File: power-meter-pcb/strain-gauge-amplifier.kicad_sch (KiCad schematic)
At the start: 19 parts, among them J5 Side A, J6 Side B, Q3 AS2302, U7 ADS1232IPW

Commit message: Cleaning up PCB back and title box
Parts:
- C12, C13, C14, C15, J5, J6, NT2, Q3, R17, R18, R19, R20, SG1, SG2, SG3, SG4, U7: PlaceOnSecondary (none) -> Yes
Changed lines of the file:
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@@
 	(title_block
 		(title "Cycling power meter FYP - Strain gauge amplifier")
-		(date "2024-04-18")
+		(date "2024-05-14")
+		(rev "V1.0")
 		(company "Monash Human Power - Jotham Gates & Oscar Varney")
-		(comment 1 "For the secondary crank, set J3 to short pins 2 and 3 and short J1 and J2.")
 	)
 	(junction
@@
 			)
 		)
+		(property "PlaceOnSecondary" "Yes"
+			(at 55.88 72.39 0)
+			(effects
+				(font
+					(size 1.27 1.27)
+				)
+				(hide yes)
+			)
+		)
 		(pin "2"
 		)
@@
 			)
 		)
+		(property "PlaceOnSecondary" "Yes"
+			(at 109.22 72.39 0)
+			(effects
+				(font
+					(size 1.27 1.27)
+				)
+				(hide yes)
+			)
+		)
 		(pin "2"
 		)
@@
 			)
 		)
+		(property "PlaceOnSecondary" "Yes"
+			(at 185.42 87.63 0)
+			(effects
+				(font
+					(size 1.27 1.27)
+				)
+				(hide yes)
+			)
+		)
 		(pin "1"
 		)
@@
 			)
 		)
+		(property "PlaceOnSecondary" "Yes"
+			(at 66.04 124.46 0)
+			(effects
+				(font
+					(size 1.27 1.27)
+				)
+				(hide yes)
+			)
+		)
 		(pin "1"
 		)
@@
 			)
 		)
+		(property "PlaceOnSecondary" "Yes"
+			(at 109.22 87.63 0)
+			(effects
+				(font
+					(size 1.27 1.27)
+				)
+				(hide yes)
+			)
+		)
 		(pin "2"
 		)
@@
 			)
 		)
+		(property "PlaceOnSecondary" "Yes"
+			(at 185.42 97.79 0)
+			(effects
+				(font
+					(size 1.27 1.27)
+				)
+				(hide yes)
+			)
+		)
 		(pin "2"
 		)
@@
 			)
 		)
+		(property "PlaceOnSecondary" "Yes"
+			(at 55.88 87.63 0)
+			(effects
+				(font
+					(size 1.27 1.27)
+				)
+				(hide yes)
+			)
+		)
 		(pin "2"
 		)
@@
 			)
 		)
+		(property "PlaceOnSecondary" "Yes"
+			(at 127 88.9 0)
+			(effects
+				(font
+					(size 1.27 1.27)
+				)
+				(hide yes)
+			)
+		)
 		(pin "1"
 		)
@@
 			)
 		)
+		(property "PlaceOnSecondary" "Yes"
+			(at 68.58 78.74 0)
+			(effects
+				(font
+					(size 1.27 1.27)
+				)
+				(hide yes)
+			)
+		)
 		(pin "3"
 		)
@@
 			)
 		)
+		(property "PlaceOnSecondary" "Yes"
+			(at 153.67 130.81 0)
+			(effects
+				(font
+					(size 1.27 1.27)
+				)
+				(hide yes)
+			)
+		)
 		(pin "1"
 		)
@@
 			)
 		)
+		(property "PlaceOnSecondary" "Yes"
+			(at 236.22 91.44 0)
+			(effects
+				(font
+					(size 1.27 1.27)
+				)
+				(hide yes)
+			)
+		)
 		(pin "1"
 		)
@@
 			)
 		)
+		(property "PlaceOnSecondary" "Yes"
+			(at 224.79 91.44 0)
+			(effects
+				(font
+					(size 1.27 1.27)
+				)
+				(hide yes)
+			)
+		)
 		(pin "1"
 		)
@@
 			)
 		)
+		(property "PlaceOnSecondary" "Yes"
+			(at 96.52 78.74 0)
+			(effects
+				(font
+					(size 1.27 1.27)
+				)
+				(hide yes)
+			)
+		)
 		(pin "3"
 		)
@@
 			)
 		)
+		(property "PlaceOnSecondary" "Yes"
+			(at 59.69 118.11 0)
+			(effects
+				(font
+					(size 1.27 1.27)
+				)
+				(hide yes)
+			)
+		)
 		(pin "1"
 		)
@@
 			)
 		)
+		(property "PlaceOnSecondary" "Yes"
+			(at 156.21 100.33 0)
+			(effects
+				(font
+					(size 1.27 1.27)
+				)
+				(hide yes)
+			)
+		)
 		(pin "18"
 		)
@@
 			)
 		)
+		(property "PlaceOnSecondary" "Yes"
+			(at 73.66 118.11 0)
+			(effects
+				(font
+					(size 1.27 1.27)
+				)
+				(hide yes)
+			)
+		)
 		(pin "1"
 		)
@@
 			(at 185.42 90.17 0)
 			(effects
+				(font
+					(size 1.27 1.27)
+				)
+				(hide yes)
+			)
+		)
+		(property "PlaceOnSecondary" "Yes"
+			(at 185.42 90.17 0)
+			(effects

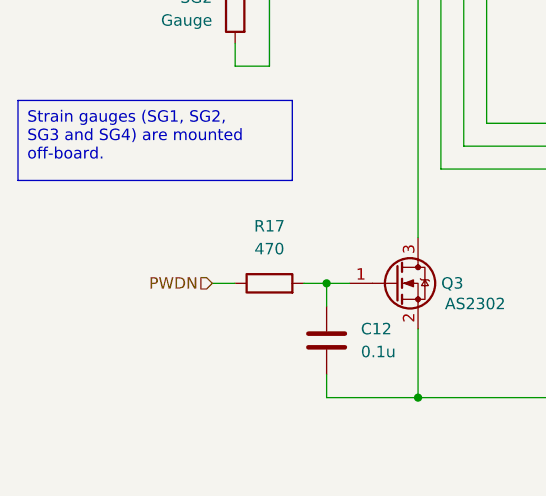
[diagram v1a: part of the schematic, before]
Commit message: Smaller PCB design started
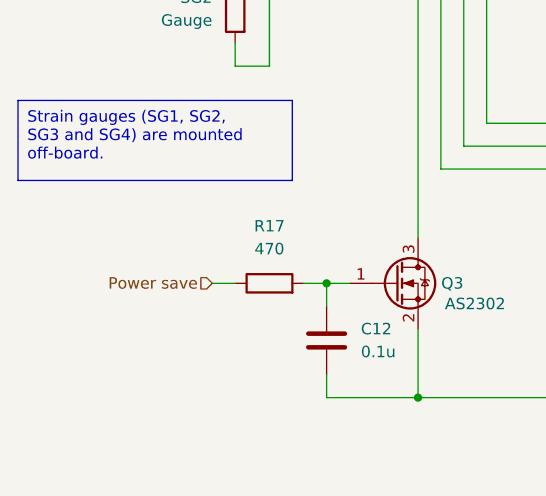
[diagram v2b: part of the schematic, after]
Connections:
- net PWDN: no longer R17.1
- new net Power save: R17.1
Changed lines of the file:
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@@
 		)
 	)
-	(hierarchical_label "PWDN"
+	(hierarchical_label "Power save"
 		(shape input)
 		(at 53.34 118.11 180)

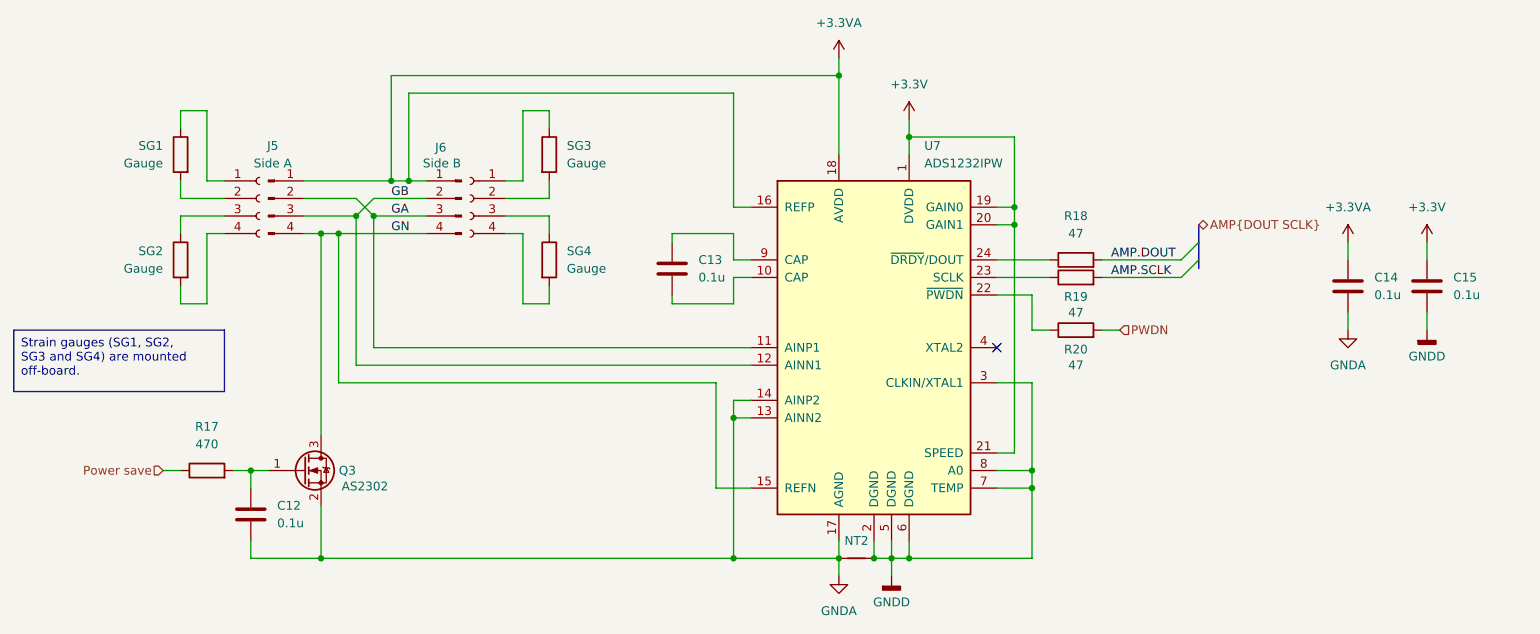
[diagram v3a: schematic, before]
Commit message: Re-centred schematics, added header for spare GPIO pins, touched up logos
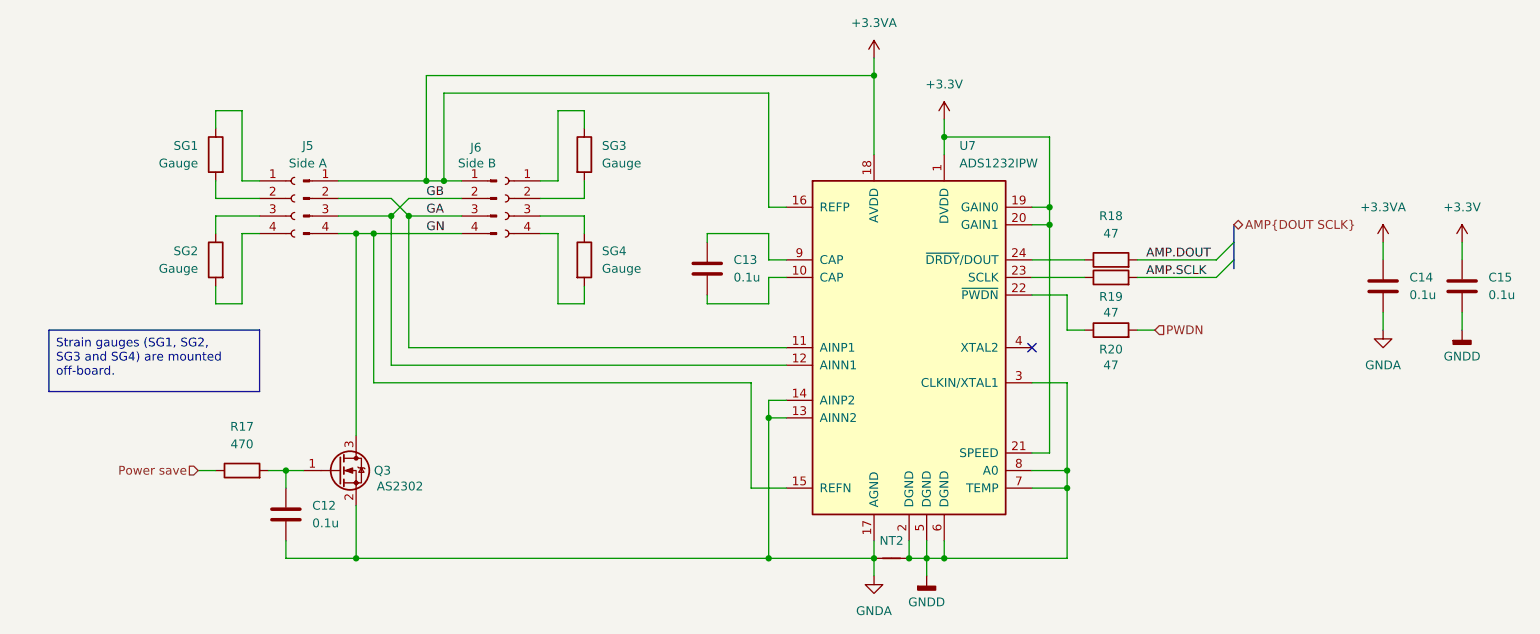
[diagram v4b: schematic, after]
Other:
- moved on the sheet: C12, C13, C14, C15, J5, J6, NT2, Q3, R17, R18, R19, R20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

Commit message: Added LED driven by temp sensor, updated numbering
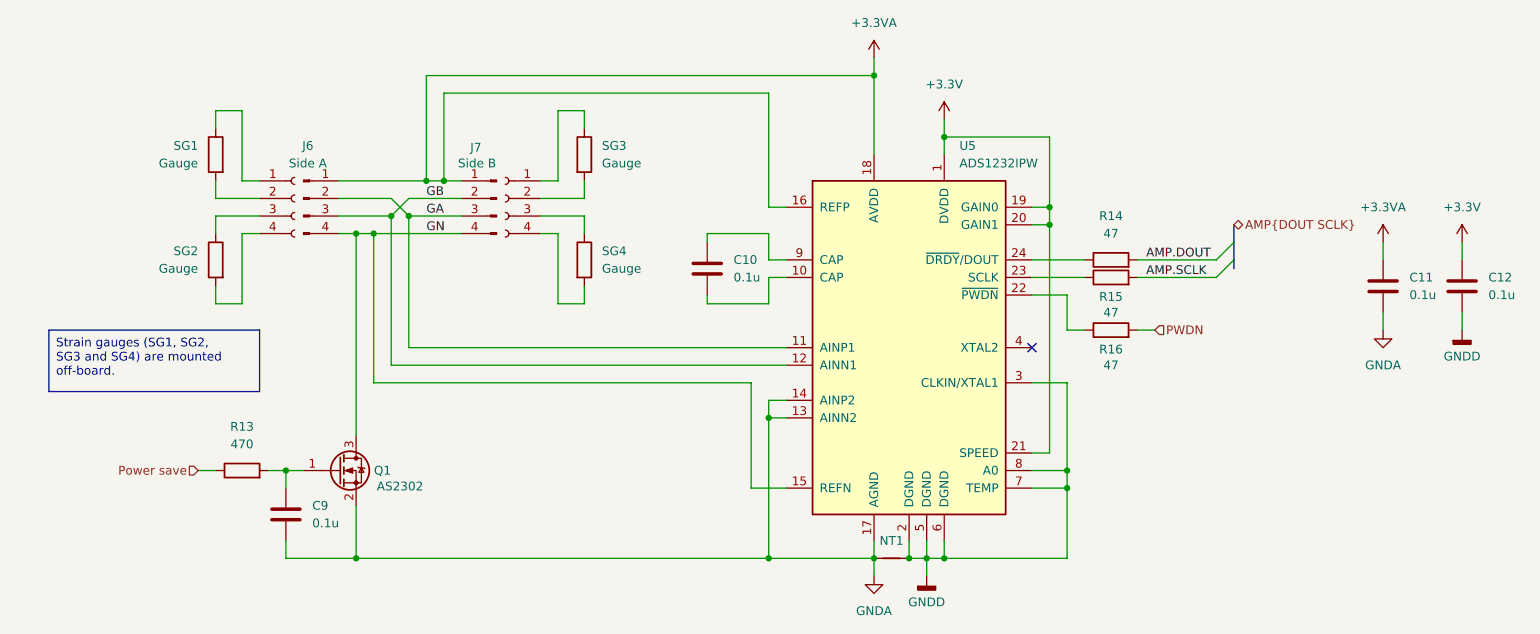
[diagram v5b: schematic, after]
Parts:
- renumbered C13 to C10, C14 to C11, C15 to C12, C12 to C9, J5 to J6, J6 to J7, NT2 to NT1, Q3 to Q1, R17 to R13, R18 to R14, R19 to R15, R20 to R16, U7 to U5
